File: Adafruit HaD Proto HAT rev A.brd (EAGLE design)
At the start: 65 x 56.5 mm, 13 parts, among them U1 CAT24C32

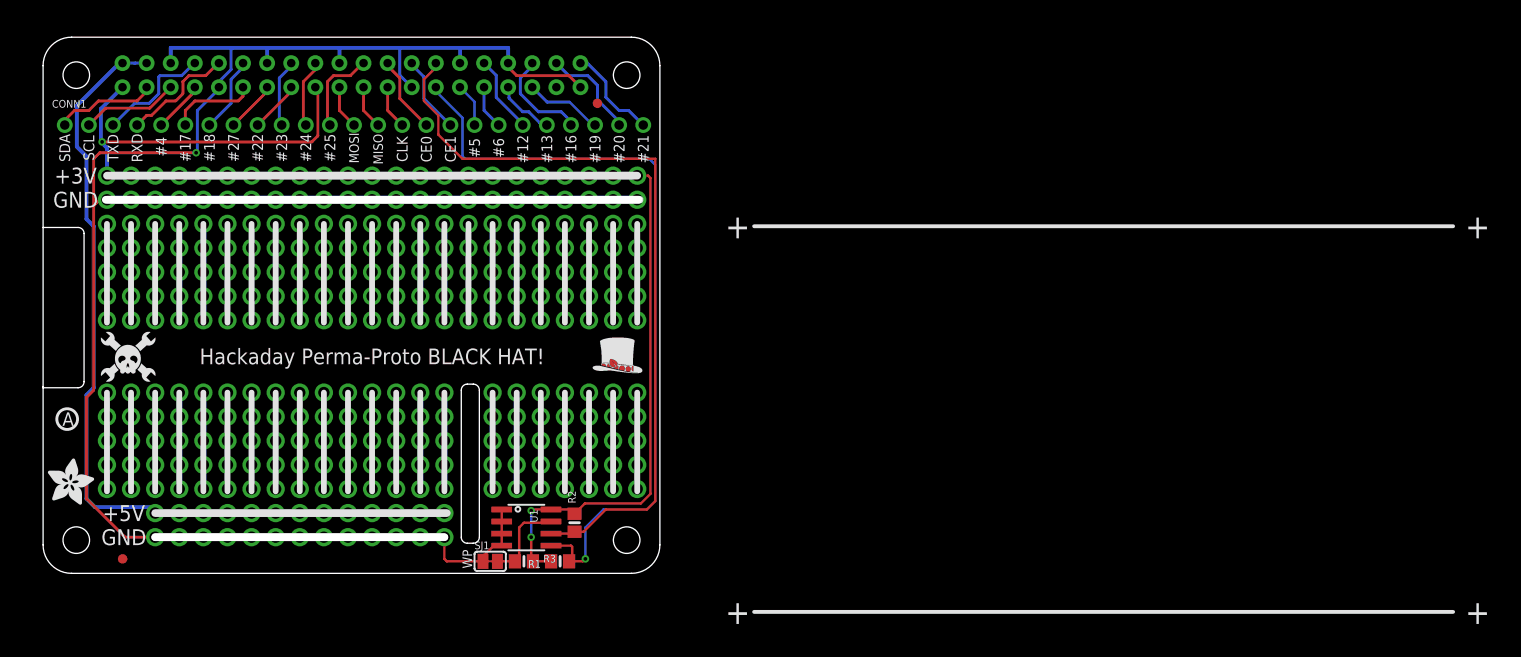
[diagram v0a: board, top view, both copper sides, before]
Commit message: ripped out proto area, added in 4xSAO connectors
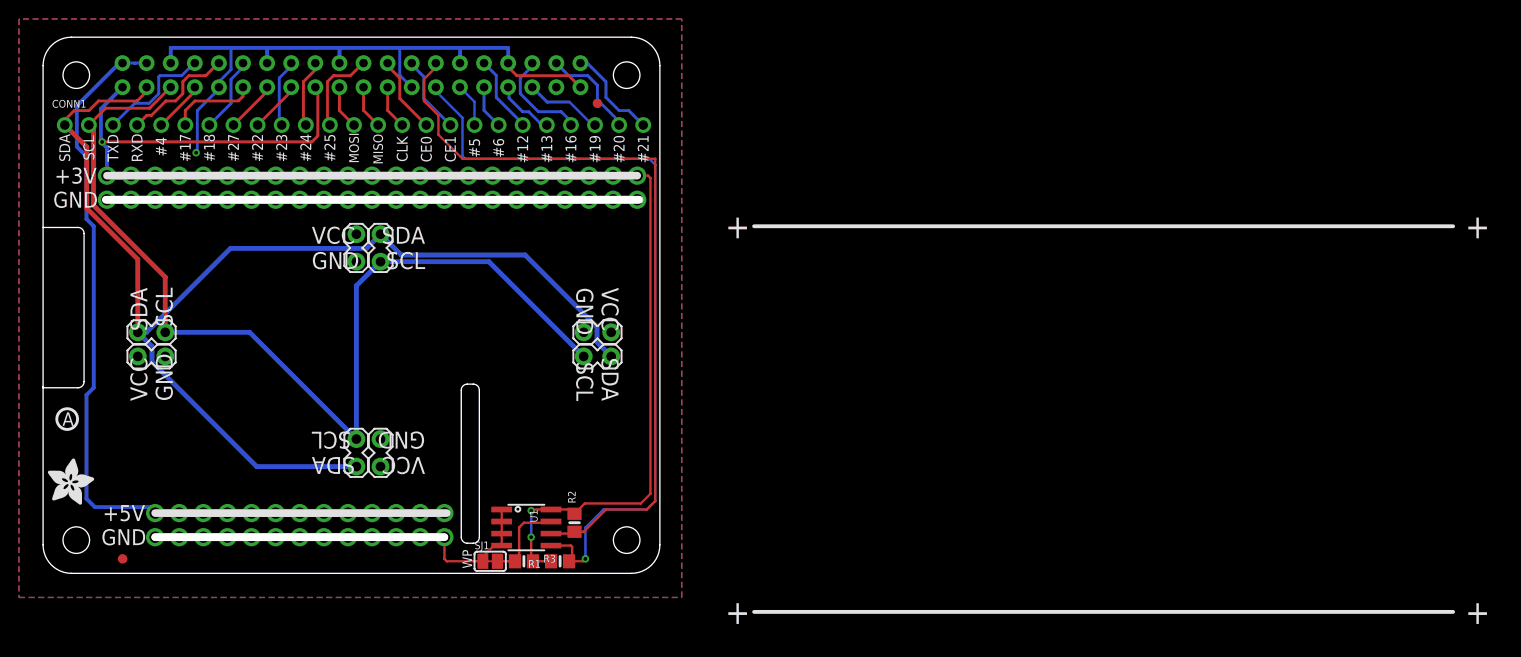
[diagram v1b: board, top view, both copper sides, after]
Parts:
- removed U$2: (no value), microbuilder:PIHATLOGO
- removed U$5: (no value), microbuilder:HAD_LOGO_200MIL
- added J1, J2, J3, J4, J5, J6, J7, J8: (no value), SparkFun-Connectors:1X02_LOCK
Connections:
- net 3.3V: now also J1.2, J3.2, J5.2, J7.2
- net GND: now also J1.1, J3.1, J5.1, J7.1
- net SCL: now also J2.1, J4.1, J6.1, J8.1
- net SDA: now also J2.2, J4.2, J6.2, J8.2
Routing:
- net SDA: track 10.8 -> 126.2 mm
- net SCL: track 10.3 -> 105.6 mm
- net GND: track 227.3 -> 169.6 mm
- net N$9: track 10.2 -> 0.00 mm, vias 5 -> 0
- net N$8: track 10.2 -> 0.00 mm, vias 5 -> 0
- net N$7: track 10.2 -> 0.00 mm, vias 5 -> 0
- net N$6: track 10.2 -> 0.00 mm, vias 5 -> 0
- net N$5: track 10.2 -> 0.00 mm, vias 5 -> 0
- net N$4: track 10.2 -> 0.00 mm, vias 5 -> 0
- net N$3: track 10.2 -> 0.00 mm, vias 5 -> 0
- net N$23: track 10.2 -> 0.00 mm, vias 5 -> 0
- net N$22: track 10.2 -> 0.00 mm, vias 5 -> 0
- net N$21: track 10.2 -> 0.00 mm, vias 5 -> 0
- net N$20: track 10.2 -> 0.00 mm, vias 5 -> 0
- net N$2: track 10.2 -> 0.00 mm, vias 5 -> 0
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- added copper zone on layer 16, net 3.3V
- added copper zone on layer 1, net GND
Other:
- board text added: "Raspberry Pi SAO HAT git.io/rpi-shat"
- board text added: "VCC SDA GND SCL"
- board text removed: "Hackaday Perma-Proto BLACK HAT!"
